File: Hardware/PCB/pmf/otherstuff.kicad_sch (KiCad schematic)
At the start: 70 parts, among them J10 Synth_power_2x5, J11 Conn_02x07_Odd_Even, J12 AudioJack2, J13 Conn_02x07_Odd_Even, J14 Conn_02x07_Odd_Even, J5 AudioJack2, J6 AudioJack2, J7 AudioJack2, J8 AudioJack2, J9 AudioJack2, M1 screw, M2 nut, M3 washer, M4 spacer, SW1 SW_Rotary12, U2 TL072

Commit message: Pre fab tweaks, Gerbers, BOM
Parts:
- removed M2: nut, symbol AO_symbols:Nut
- added B1: Board, AO_tht:Board_Marker, symbol AO_symbols:Board
- added J15, J16: DIP-8, symbol AO_symbols:DIP-8
- added J17: DIP-14, symbol AO_symbols:DIP-14
- added J18: DIP-18, symbol AO_symbols:DIP-18
- added M10, M11: washer, symbol AO_symbols:Washer
- added M12, M13: spacer, symbol AO_symbols:Spacer
- added M5, M6, M7, M8, M9: screw, symbol AO_symbols:Screw

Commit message: BOM
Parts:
- added W1: Ribbon_Cable, symbol AO_symbols:Ribbon_Cable
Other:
- note added: "Ribbon cable"
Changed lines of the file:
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@@
+    (effects (font (size 1.27 1.27)) (justify left bottom))
+  )
+  (text "Ribbon cable" (at 220.98 55.88 0)
     (effects (font (size 1.27 1.27)) (justify left bottom))
   )
@@
         )
       )
+    )
+  )
+  (symbol (lib_id "AO_symbols:Ribbon_Cable") (at 245.11 163.83 0) (unit 1)
+    (in_bom yes) (on_board no) (dnp no) (fields_autoplaced)
+    (property "Reference" "W1" (at 245.11 163.83 0)
+      (effects (font (size 1.27 1.27)) hide)
+    )
+    (property "Value" "Ribbon_Cable" (at 245.11 163.83 0)
+      (effects (font (size 1.27 1.27)) hide)
+    )
+    (property "Footprint" "" (at 245.364 163.83 0)
+      (effects (font (size 1.27 1.27)) hide)
+    )
+    (property "Datasheet" "" (at 245.364 163.83 0)
+      (effects (font (size 1.27 1.27)) hide)
+    )
+    (property "Description" "14 conductor 1.27 mm pitch ribbon cable 12 cm" (at 245.11 163.83 0)
+      (effects (font (size 1.27 1.27)) hide)
+    )
+    (instances
+      (project "pmf"
+        (path "/1fce46f5-2003-4c7e-915f-b9b7dfc679d7/a180c6ca-d86a-4fef-be09-a6b0b94046eb"
+          (reference "W1") (unit 1)
+        )
+      )

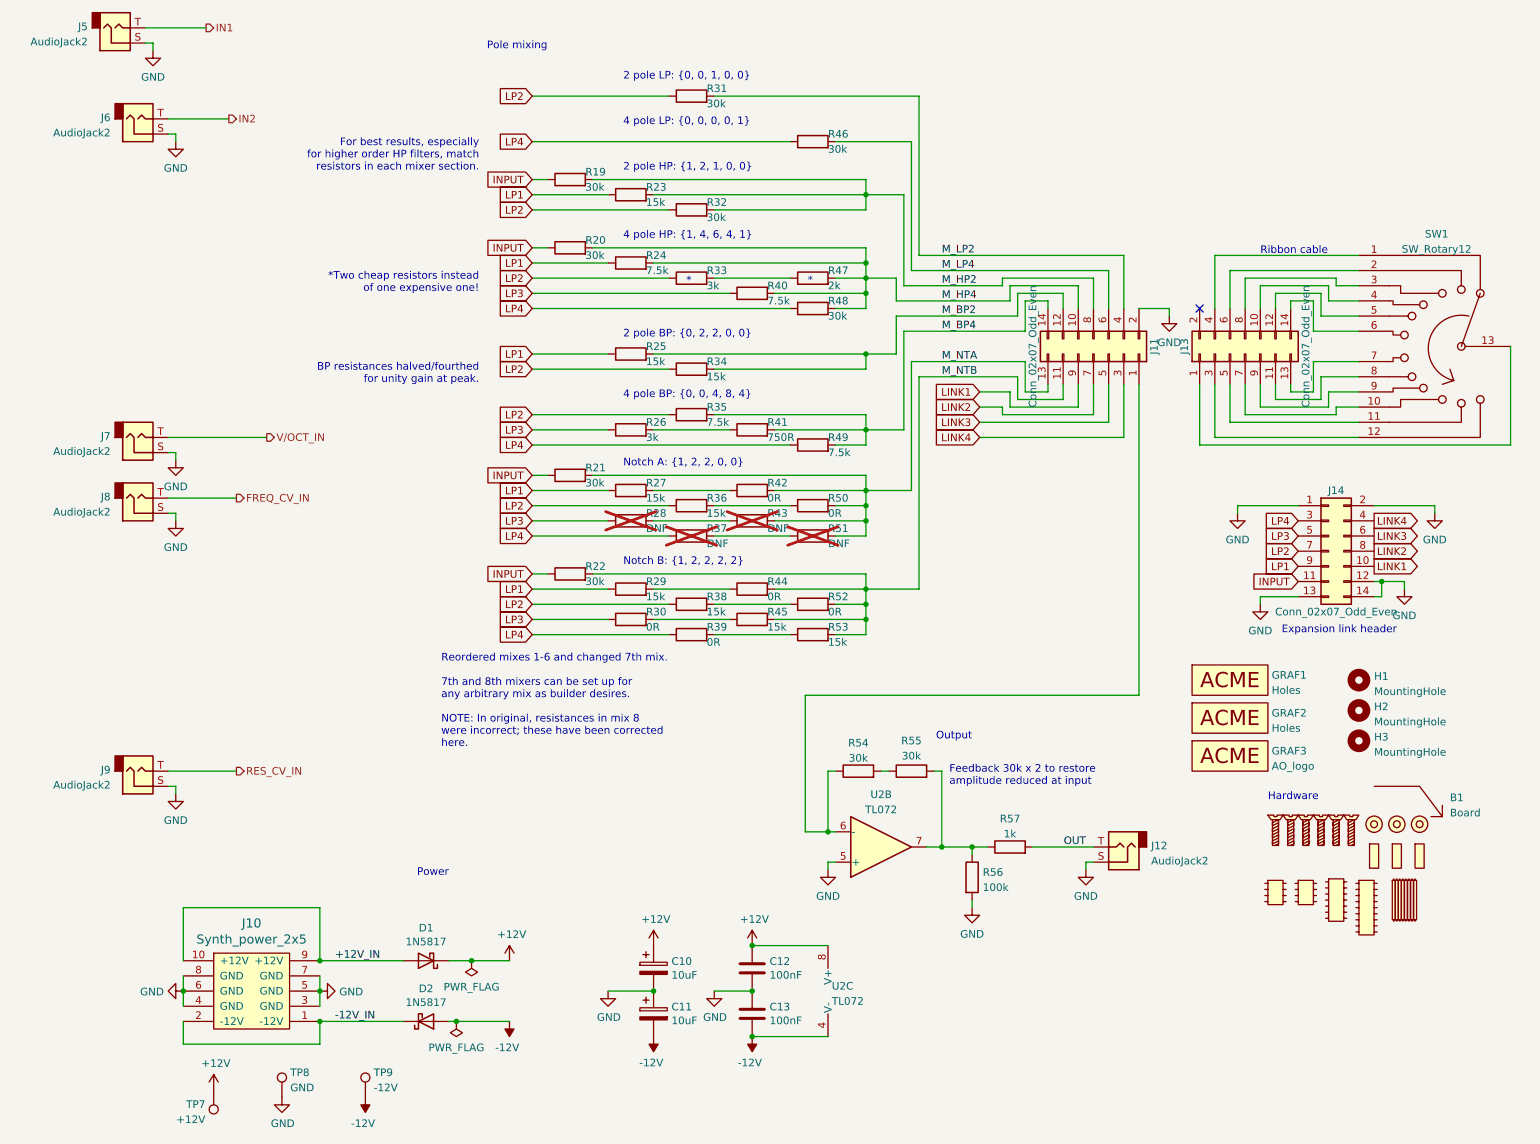
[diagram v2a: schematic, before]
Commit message: Text boxes
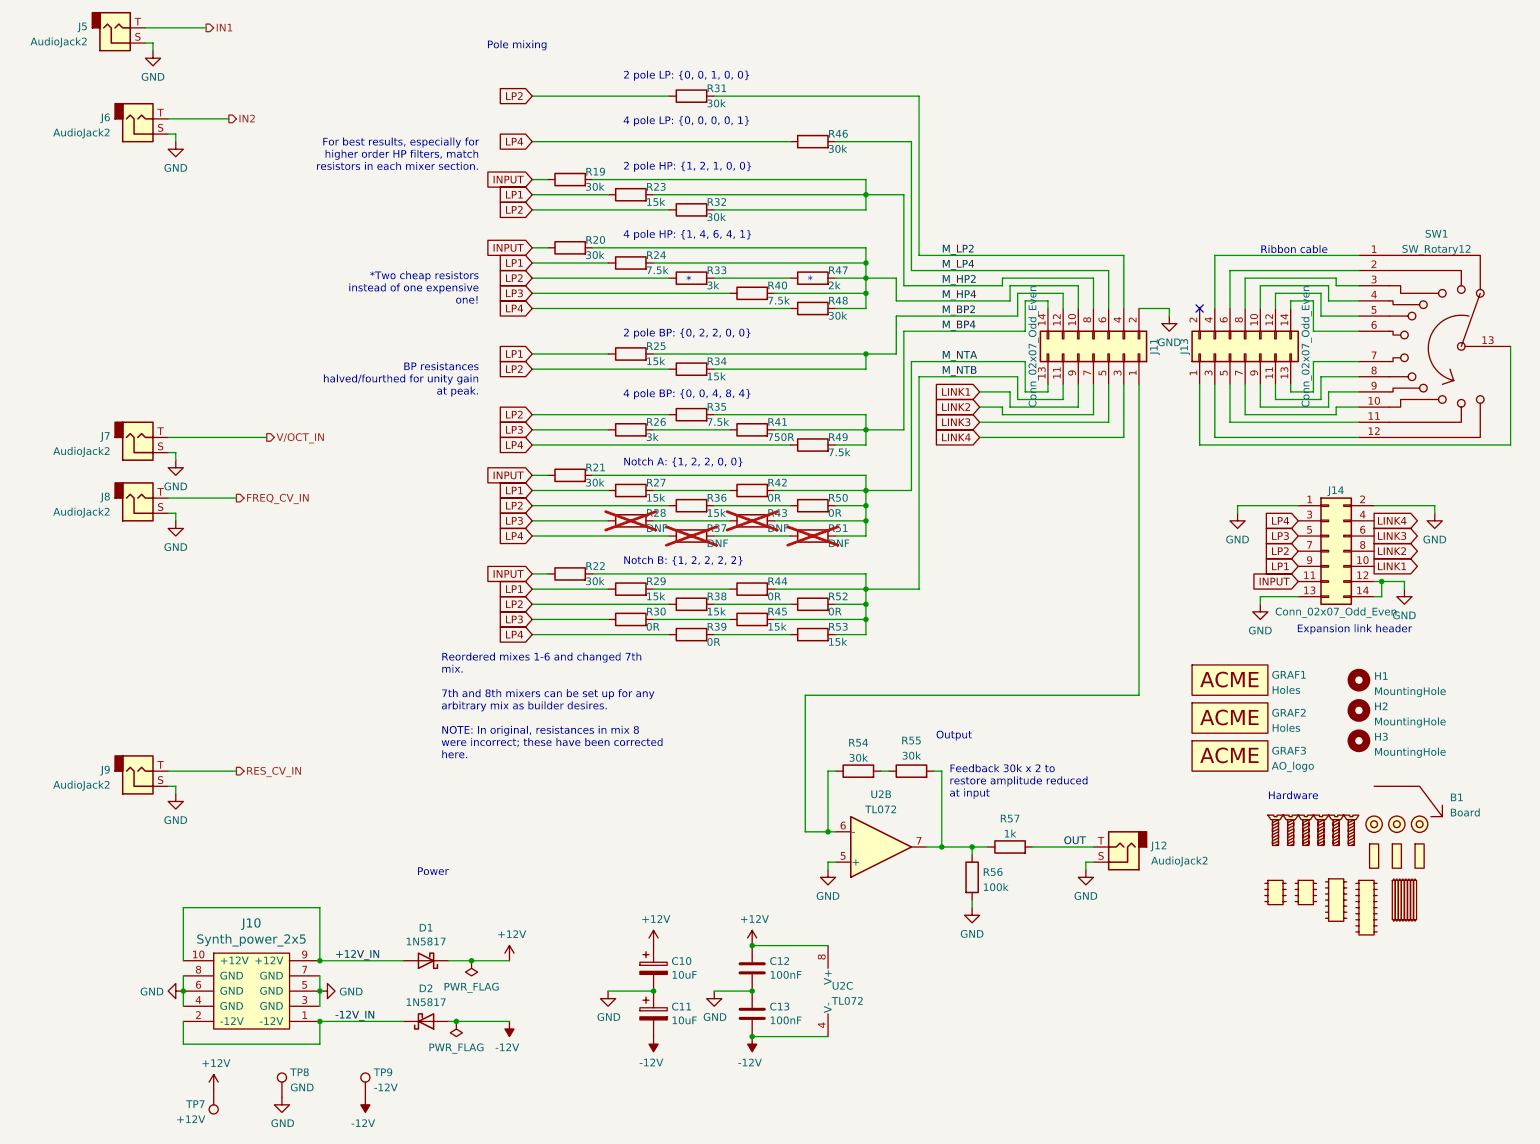
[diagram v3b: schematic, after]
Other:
- note removed: "*Two cheap resistors instead of one expensive one!"
- note removed: "BP resistances halved/fourthed for unity gain at peak."
- note removed: "Feedback 30k x 2 to restore amplitude reduced at input"
- note removed: "For best results, especially for higher order HP filters, match resistors in each mixer section."
- note removed: "Reordered mixes 1-6 and changed 7th mix. 7th and 8th mixers can be set up for any arbitrary mix as builder desires. NOTE: In original, resistances in mix 8 were incorrect; these have been corrected here."
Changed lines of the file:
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@@
     (stroke (width 0) (type default))
+  )
+  (text_box "BP resistances halved/fourthed for unity gain at peak."
+    (at 58.7103 72.7296 0) (size 32.4757 5.7564)
+    (stroke (width -0.0001) (type default))
+    (fill (type none))
+    (effects (font (size 1.27 1.27)) (justify right top))
+  )
+  (text_box "*Two cheap resistors instead of one expensive one!"
+    (at 61.5163 57.4896 0) (size 29.6697 5.7564)
+    (stroke (width -0.0001) (type default))
+    (fill (type none))
+    (effects (font (size 1.27 1.27)) (justify right top))
+  )
+  (text_box "Reordered mixes 1-6 and changed 7th mix.\n\n7th and 8th mixers can be set up for any arbitrary mix as builder desires.\n\nNOTE: In original, resistances in mix 8 were incorrect; these have been corrected here.\n"
+    (at 82.804 121.3452 0) (size 44.1717 18.1008)
+    (stroke (width -0.0001) (type default))
+    (fill (type none))
+    (effects (font (size 1.27 1.27)) (justify left top))
+  )
+  (text_box "For best results, especially for higher order HP filters, match resistors in each mixer section."
+    (at 56.9685 35.1122 0) (size 34.2175 7.8138)
+    (stroke (width -0.0001) (type default))
+    (fill (type none))
+    (effects (font (size 1.27 1.27)) (justify right top))
+  )
+  (text_box "Feedback 30k x 2 to restore amplitude reduced at input"
+    (at 167.894 140.0396 0) (size 29.0771 5.7564)
+    (stroke (width -0.0001) (type default))
+    (fill (type none))
+    (effects (font (size 1.27 1.27)) (justify left top))
   )
   (text "Pole mixing" (at 101.6 21.59 0)
@@
   )
   (text "2 pole BP: {0, 2, 2, 0, 0}" (at 114.3 69.85 0)
-    (effects (font (size 1.27 1.27)) (justify left bottom))
-  )
-  (text "Feedback 30k x 2 to restore\namplitude reduced at input"
-    (at 168.91 144.78 0)
     (effects (font (size 1.27 1.27)) (justify left bottom))
   )
@@
     (effects (font (size 1.27 1.27)) (justify left bottom))
   )
-  (text "For best results, especially\nfor higher order HP filters, match\nresistors in each mixer section."
-    (at 90.17 41.91 0)
-    (effects (font (size 1.27 1.27)) (justify right bottom))
-  )
   (text "Output" (at 172.72 137.16 0)
-    (effects (font (size 1.27 1.27)) (justify right bottom))
-  )
-  (text "BP resistances halved/fourthed\nfor unity gain at peak."
-    (at 90.17 77.47 0)
-    (effects (font (size 1.27 1.27)) (justify right bottom))
-  )
-  (text "*Two cheap resistors instead\nof one expensive one!"
-    (at 90.17 62.23 0)
     (effects (font (size 1.27 1.27)) (justify right bottom))
   )
@@
     (effects (font (size 1.27 1.27)) (justify left bottom))
   )
-  (text "Expansion link header\n" (at 243.84 119.38 0)
+  (text "Expansion link header\n" (at 246.38 119.38 0)
     (effects (font (size 1.27 1.27)) (justify right bottom))
   )
@@
     (effects (font (size 1.27 1.27)) (justify right bottom))
   )
-  (text "Reordered mixes 1-6 and changed 7th mix.\n\n7th and 8th mixers can be set up for \nany arbitrary mix as builder desires.\n\nNOTE: In original, resistances in mix 8\nwere incorrect; these have been corrected\nhere.\n"
-    (at 83.82 138.43 0)
-    (effects (font (size 1.27 1.27)) (justify left bottom))
-  )
   (label "M_LP2" (at 167.64 55.88 0) (fields_autoplaced)

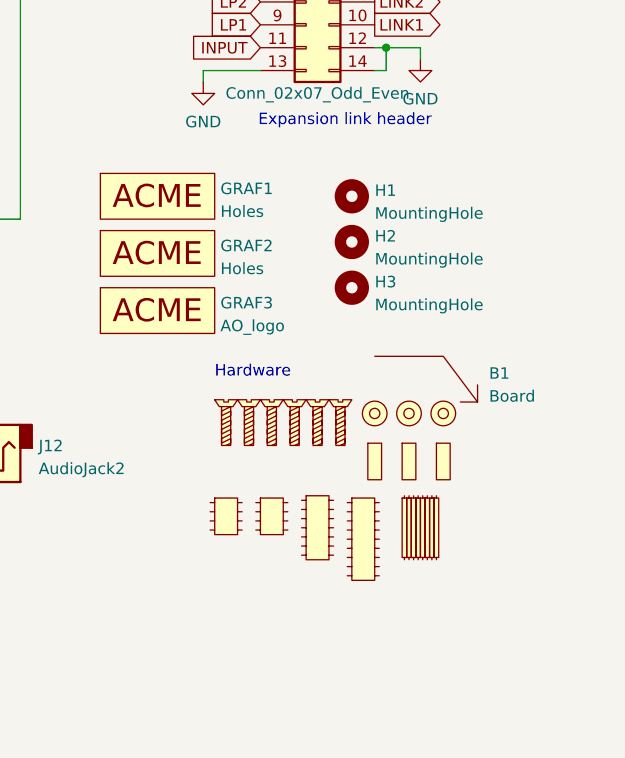
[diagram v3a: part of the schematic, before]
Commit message: Knobs, new hardware refs, improved BOM format
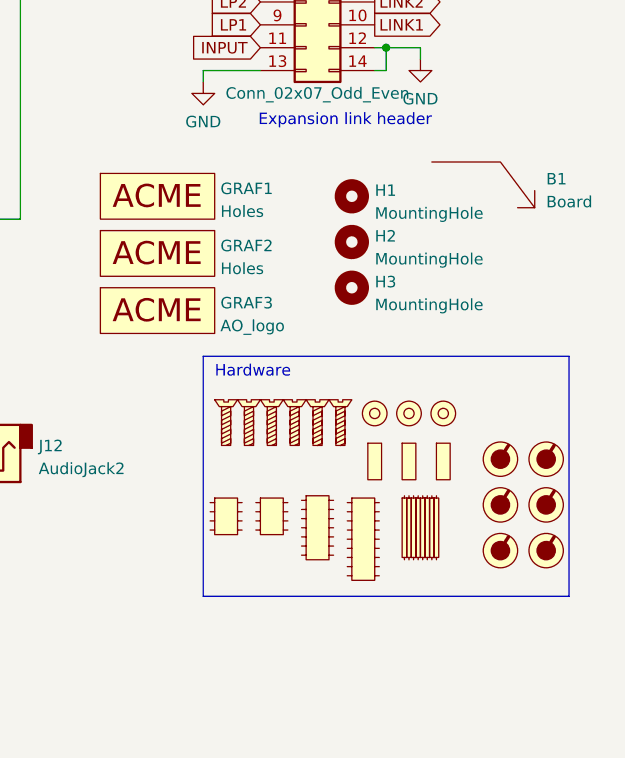
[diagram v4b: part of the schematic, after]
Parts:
- added ZKN1: Knob_MF-A04, symbol AO_symbols:Knob
- added ZKN2, ZKN3, ZKN4, ZKN5, ZKN6: Knob_MF-A03, symbol AO_symbols:Knob
- ZSC1: renamed from M1; value screw -> Screw
- ZSC2: renamed from M5; value screw -> Screw
- ZSC3: renamed from M6; value screw -> Screw
- ZSC4: renamed from M7; value screw -> Screw
- ZSC5: renamed from M8; value screw -> Screw
- ZSC6: renamed from M9; value screw -> Screw
- ZSP1: renamed from M12; value spacer -> Spacer
- ZSP2: renamed from M13; value spacer -> Spacer
- ZSP3: renamed from M4; value spacer -> Spacer
- ZWA1: renamed from M10; value washer -> Washer
- ZWA2: renamed from M11; value washer -> Washer
- ZWA3: renamed from M3; value washer -> Washer
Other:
- moved on the sheet: B1

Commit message: rm omit from BOM and board
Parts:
- R45, R53: now in the parts list
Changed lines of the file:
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@@
   )
   (symbol (lib_id "AO_symbols:R") (at 135.89 116.84 90) (unit 1)
-    (in_bom no) (on_board yes) (dnp no)
+    (in_bom yes) (on_board yes) (dnp no)
     (property "Reference" "R45" (at 138.43 115.57 90)
       (effects (font (size 1.27 1.27)) (justify right))
@@
   )
   (symbol (lib_id "AO_symbols:R") (at 146.05 119.38 90) (unit 1)
-    (in_bom no) (on_board yes) (dnp no)
+    (in_bom yes) (on_board yes) (dnp no)
     (property "Reference" "R53" (at 148.59 118.11 90)
       (effects (font (size 1.27 1.27)) (justify right))
